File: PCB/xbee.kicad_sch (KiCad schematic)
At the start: 8 parts

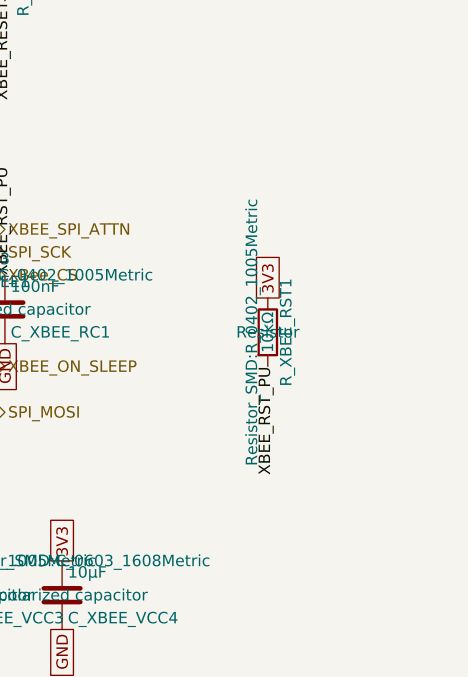
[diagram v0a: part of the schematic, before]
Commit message: fix: add pull-up on XBee SPI_ATTN pin
SPI_ATTN doubles as the XBee3's BOOTMODE strap; Digi's hardware
reference manual (doc 90001543) says not to let it be tied/pulled low
at reset. R_XBEE_ATTN_PU1 (10kΩ to 3V3) holds it high before firmware
configures the pin, matching the existing R_XBEE_RST1 pull-up pattern
on RESET.

Verified via kicad-cli: the new resistor lands on the XBEE_SPI_ATTN
net alongside U_XBEE1 pin 19 and the MCU's GPIO15, and ERC is clean.

Co-Authored-By: Claude Sonnet 5 <noreply@anthropic.com>
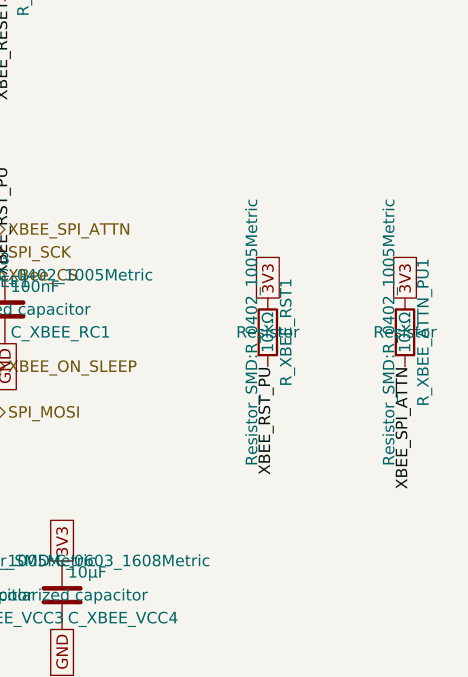
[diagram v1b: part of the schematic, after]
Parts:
- added R_XBEE_ATTN_PU1: 10kΩ, Resistor_SMD:R_0402_1005Metric, symbol Device:R
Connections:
- net 3V3: now also R_XBEE_ATTN_PU1.1
- net XBEE_SPI_ATTN: now also R_XBEE_ATTN_PU1.2
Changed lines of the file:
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@@
+		)
+	)
+	(label "XBEE_SPI_ATTN"
+		(at 210.82 114.3 270)
+		(effects
+			(font
+				(size 1.27 1.27)
+			)
+			(justify right)
 		)
 	)
@@
 		(property "Intersheetrefs" "${INTERSHEET_REFS}"
 			(at 195.58 106.68 0)
+			(hide yes)
+			(show_name no)
+			(do_not_autoplace no)
+			(effects
+				(font
+					(size 1.27 1.27)
+				)
+			)
+		)
+	)
+	(global_label "3V3"
+		(shape passive)
+		(at 210.82 106.68 90)
+		(fields_autoplaced yes)
+		(effects
+			(font
+				(size 1.27 1.27)
+			)
+			(justify left)
+		)
+		(property "Intersheetrefs" "${INTERSHEET_REFS}"
+			(at 210.82 106.68 0)
 			(hide yes)
 			(show_name no)
@@
 					(unit 1)
 				)
+			)
+		)
+	)
+	(symbol
+		(lib_id "Device:R")
+		(at 210.82 110.49 0)
+		(unit 1)
+		(body_style 1)
+		(exclude_from_sim no)
+		(in_bom yes)
+		(on_board yes)
+		(in_pos_files yes)
+		(dnp no)
+		(fields_autoplaced yes)
+		(property "Reference" "R_XBEE_ATTN_PU1"
+			(at 212.852 110.49 90)
+			(show_name no)
+			(do_not_autoplace no)
+			(effects
+				(font
+					(size 1.27 1.27)
+				)
+			)
+		)
+		(property "Value" "10kΩ"
+			(at 210.82 110.49 90)
+			(show_name no)
+			(do_not_autoplace no)
+			(effects
+				(font
+					(size 1.27 1.27)
+				)
+			)
+		)
+		(property "Footprint" "Resistor_SMD:R_0402_1005Metric"
+			(at 209.042 110.49 90)
+			(show_name no)
+			(do_not_autoplace no)
+			(effects
+				(font
+					(size 1.27 1.27)
+				)
+			)
+		)
+		(property "Datasheet" ""
+			(at 210.82 110.49 0)
+			(show_name no)
+			(do_not_autoplace no)
+			(effects
+				(font
+					(size 1.27 1.27)
+				)
+			)
+		)
+		(property "Description" "Resistor"
+			(at 210.82 110.49 0)
+			(show_name no)
+			(do_not_autoplace no)
+			(effects
+				(font
+					(size 1.27 1.27)
+				)
+			)
+		)
+		(property "MF" "Yageo"
+			(at 0 0 0)
+			(hide yes)
+			(show_name no)
+			(do_not_autoplace no)
+			(effects
+				(font
+					(size 1.27 1.27)
+				)
+			)
+		)
+		(property "Manufacturer_Part_Number" "RC0402FR-0710KL"
+			(at 0 0 0)
+			(hide yes)
+			(show_name no)
+			(do_not_autoplace no)
+			(effects
+				(font
+					(size 1.27 1.27)
+				)
+			)
+		)
+		(pin "1"
+		)
+		(pin "2"
+		)
+		(instances
+			(project "snips_controller"
+				(path "/21935953-32a0-46ad-8079-8177920c6978/4f95850f-f8fc-4b0b-b598-e710af0bb56d"
+					(reference "R_XBEE_ATTN_PU1")
+					(unit 1)
+				)

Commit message: task: write matched LCSC part numbers into the schematic
Adds scripts/apply_lcsc_fields.py, which clones each symbol's existing
Manufacturer_Part_Number property (same indentation/effects) into a new
'LCSC' field with the matched code -- the field name the Fabrication
Toolkit plugin already installed in this repo recognizes for JLCPCB BOM
matching.

Applied the 31 confirmed matches from jlc_match.py across all sheets
(68 individual references). C_BUCK_OUT1 and R_ISET1 are left without an
LCSC field -- JLC doesn't stock those exact Yageo part numbers, to be
sorted out separately.

Verified: kicad-cli sch export bom round-trips every LCSC value
correctly, and ERC reports 0 violations.

Also switched jlc_match.py's BOM export to unranged references so each
match maps cleanly to individual schematic symbols.

Co-Authored-By: Claude Sonnet 5 <noreply@anthropic.com>
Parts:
- C_XBEE_RC1, C_XBEE_VCC1: LCSC (none) -> C131394
- C_XBEE_VCC2: LCSC (none) -> C106215
- C_XBEE_VCC3: LCSC (none) -> C60137
- C_XBEE_VCC4: LCSC (none) -> C2936601
- R_XBEE_ATTN_PU1, R_XBEE_RST1: LCSC (none) -> C60490
- R_XBEE_RC1: LCSC (none) -> C106232
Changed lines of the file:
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@@
+			)
+		)
+		(property "LCSC" "C60137"
+			(at 0 0 0)
+			(hide yes)
+			(show_name no)
+			(do_not_autoplace no)
+			(effects
+				(font
+					(size 1.27 1.27)
+				)
 			)
 		)
@@
 			)
 		)
+		(property "LCSC" "C106215"
+			(at 0 0 0)
+			(hide yes)
+			(show_name no)
+			(do_not_autoplace no)
+			(effects
+				(font
+					(size 1.27 1.27)
+				)
+			)
+		)
 		(pin "1"
 		)
@@
 			)
 		)
+		(property "LCSC" "C2936601"
+			(at 0 0 0)
+			(hide yes)
+			(show_name no)
+			(do_not_autoplace no)
+			(effects
+				(font
+					(size 1.27 1.27)
+				)
+			)
+		)
 		(pin "1"
 		)
@@
 			)
 		)
+		(property "LCSC" "C131394"
+			(at 0 0 0)
+			(hide yes)
+			(show_name no)
+			(do_not_autoplace no)
+			(effects
+				(font
+					(size 1.27 1.27)
+				)
+			)
+		)
 		(pin "1"
 		)
@@
 			)
 		)
+		(property "LCSC" "C60490"
+			(at 0 0 0)
+			(hide yes)
+			(show_name no)
+			(do_not_autoplace no)
+			(effects
+				(font
+					(size 1.27 1.27)
+				)
+			)
+		)
 		(pin "1"
 		)
@@
 			)
 		)
+		(property "LCSC" "C60490"
+			(at 0 0 0)
+			(hide yes)
+			(show_name no)
+			(do_not_autoplace no)
+			(effects
+				(font
+					(size 1.27 1.27)
+				)
+			)
+		)
 		(pin "1"
 		)
@@
 			)
 		)
+		(property "LCSC" "C106232"
+			(at 0 0 0)
+			(hide yes)
+			(show_name no)
+			(do_not_autoplace no)
+			(effects
+				(font
+					(size 1.27 1.27)
+				)
+			)
+		)
 		(pin "1"
 		)
@@
 			(at 0 0 0)
 			(hide yes)
+			(show_name no)
+			(do_not_autoplace no)
+			(effects
+				(font
+					(size 1.27 1.27)
+				)
+			)
+		)
+		(property "LCSC" "C131394"
+			(at 0 0 0)
+			(hide yes)

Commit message: task: alert on Basic-library alternatives during JLC part matching (#33)
* task: alert on Basic-library alternatives during JLC part matching

JLC's "Extended" library carries a per-unique-part setup fee on top of
unit price; "Basic" doesn't. That fee doesn't amortize well on a board
with many distinct low-quantity parts -- confirmed the hard way: our
first real JLCPCB assembly quote came back at $333.84 vs PCBWay's
~$190 for the same order, and all 33 of our matched parts were
Extended.

jlc_match.py now does a secondary search for a same-value/same-package
Basic-library part whenever the real match lands on Extended, and
flags it in the report (new BasicAlt column + a Status alert) rather
than silently leaving it. On the current board this surfaces 11
plausible Basic-library swaps (common resistor/cap values, and the
generic 1N4148W diode and 2N7002 MOSFET, which are industry-standard
parts many brands stock identically).

This is alert-only, same as the rest of this script -- it doesn't
touch the schematic. Spot-checked 4 of the 11 suggestions directly
against JLC's catalog to confirm value/package actually match, not
just a keyword hit.

Co-Authored-By: Claude Sonnet 5 <noreply@anthropic.com>

* fix: two correctness bugs in Basic-library alternative matching

1. find_basic_alternative() trusted the raw keyword-search hit without
   verifying the candidate's actual value -- JLC's fuzzy full-text search
   can return a wrong-value part that just shares digits (e.g. searching
   "100 0402" surfaced a 1kΩ resistor, EIA code "1001", as a false match
   for a 100Ω part). Now parses and compares the actual numeric value
   (with unit) before accepting a candidate; falls back to exact
   model-name matching for non-numeric values (generic diode/transistor
   part families like "1N4148W", "2N7002").

2. The new value parser's regex required the unit to be the first
   character of the string, but JLC resistor descriptions carry a
   Chinese prefix ("厚膜电阻 10kΩ ±1%" = "thi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
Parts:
- C_XBEE_RC1, C_XBEE_VCC1: LCSC C131394 -> C1525; MF Yageo -> Samsung Electro-Mechanics; Manufacturer_Part_Number CC0402KRX7R9BB104 -> CL05B104KO5NNNC
- C_XBEE_VCC2: LCSC C106215 -> C15849; MF Yageo -> Samsung Electro-Mechanics; Manufacturer_Part_Number CC0603KRX5R7BB105 -> CL10A105KB8NNNC
- C_XBEE_VCC3: LCSC C60137 -> C1567; MF Yageo -> FH (Guangdong Fenghua Advanced Tech); Manufacturer_Part_Number CC0402JRNPO9BN470 -> 0402CG470J500NT
- C_XBEE_VCC4: LCSC C2936601 -> C19702; MF Yageo -> Samsung Electro-Mechanics; Manufacturer_Part_Number CC0603KRX5R7BB106 -> CL10A106KP8NNNC
- R_XBEE_ATTN_PU1, R_XBEE_RST1: LCSC C60490 -> C25744; MF Yageo -> UNI-ROYAL(Uniroyal Elec); Manufacturer_Part_Number RC0402FR-0710KL -> 0402WGF1002TCE
- R_XBEE_RC1: LCSC C106232 -> C25076; MF Yageo -> UNI-ROYAL(Uniroyal Elec); Manufacturer_Part_Number RC0402FR-07100RL -> 0402WGF1000TCE
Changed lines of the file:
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@@
 			)
 		)
-		(property "MF" "Yageo"
-			(at 0 0 0)
-			(hide yes)
-			(show_name no)
-			(do_not_autoplace no)
-			(effects
-				(font
-					(size 1.27 1.27)
-				)
-			)
-		)
-		(property "Manufacturer_Part_Number" "CC0402JRNPO9BN470"
-			(at 0 0 0)
-			(hide yes)
-			(show_name no)
-			(do_not_autoplace no)
-			(effects
-				(font
-					(size 1.27 1.27)
-				)
-			)
-		)
-		(property "LCSC" "C60137"
+		(property "MF" "FH (Guangdong Fenghua Advanced Tech)"
+			(at 0 0 0)
+			(hide yes)
+			(show_name no)
+			(do_not_autoplace no)
+			(effects
+				(font
+					(size 1.27 1.27)
+				)
+			)
+		)
+		(property "Manufacturer_Part_Number" "0402CG470J500NT"
+			(at 0 0 0)
+			(hide yes)
+			(show_name no)
+			(do_not_autoplace no)
+			(effects
+				(font
+					(size 1.27 1.27)
+				)
+			)
+		)
+		(property "LCSC" "C1567"
 			(at 0 0 0)
 			(hide yes)
@@
 			)
 		)
-		(property "MF" "Yageo"
-			(at 0 0 0)
-			(hide yes)
-			(show_name no)
-			(do_not_autoplace no)
-			(effects
-				(font
-					(size 1.27 1.27)
-				)
-			)
-		)
-		(property "Manufacturer_Part_Number" "CC0603KRX5R7BB105"
-			(at 0 0 0)
-			(hide yes)
-			(show_name no)
-			(do_not_autoplace no)
-			(effects
-				(font
-					(size 1.27 1.27)
-				)
-			)
-		)
-		(property "LCSC" "C106215"
+		(property "MF" "Samsung Electro-Mechanics"
+			(at 0 0 0)
+			(hide yes)
+			(show_name no)
+			(do_not_autoplace no)
+			(effects
+				(font
+					(size 1.27 1.27)
+				)
+			)
+		)
+		(property "Manufacturer_Part_Number" "CL10A105KB8NNNC"
+			(at 0 0 0)
+			(hide yes)
+			(show_name no)
+			(do_not_autoplace no)
+			(effects
+				(font
+					(size 1.27 1.27)
+				)
+			)
+		)
+		(property "LCSC" "C15849"
 			(at 0 0 0)
 			(hide yes)
@@
 			)
 		)
-		(property "MF" "Yageo"
-			(at 0 0 0)
-			(hide yes)
-			(show_name no)
-			(do_not_autoplace no)
-			(effects
-				(font
-					(size 1.27 1.27)
-				)
-			)
-		)
-		(property "Manufacturer_Part_Number" "CC0603KRX5R7BB106"
-			(at 0 0 0)
-			(hide yes)
-			(show_name no)
-			(do_not_autoplace no)
-			(effects
-				(font
-					(size 1.27 1.27)
-				)
-			)
-		)
-		(property "LCSC" "C2936601"
+		(property "MF" "Samsung Electro-Mechanics"
+			(at 0 0 0)
+			(hide yes)
+			(show_name no)
+			(do_not_autoplace no)
+			(effects
+				(font
+					(size 1.27 1.27)
+				)
+			)
+		)
+		(property "Manufacturer_Part_Number" "CL10A106KP8NNNC"
+			(at 0 0 0)
+			(hide yes)
+			(show_name no)
+			(do_not_autoplace no)
+			(effects
+				(font
+					(size 1.27 1.27)
+				)
+			)
+		)
+		(property "LCSC" "C19702"
 			(at 0 0 0)
 			(hide yes)
@@
 			)
 		)
-		(property "MF" "Yageo"
-			(at 0 0 0)
-			(hide yes)
-			(show_name no)
-			(do_not_autoplace no)
-			(effects
-				(font
-					(size 1.27 1.27)
-				)
-			)
-		)
-		(property "Manufacturer_Part_Number" "CC0402KRX7R9BB104"
-			(at 0 0 0)
-			(hide yes)
-			(show_name no)
-			(do_not_autoplace no)
-			(effects
-				(font
-					(size 1.27 1.27)
-				)
-			)
-		)
-		(property "LCSC" "C131394"
+		(property "MF" "Samsung Electro-Mechanics"
+			(at 0 0 0)
+			(hide yes)
+			(show_name no)
+			(do_not_autoplace no)
+			(effects
+				(font
+					(size 1.27 1.27)
+				)
+			)
+		)
+		(property "Manufacturer_Part_Number" "CL05B104KO5NNNC"
+			(at 0 0 0)
+			(hide yes)
+			(show_name no)
+			(do_not_autoplace no)
+			(effects
+				(font
+					(size 1.27 1.27)
+				)
+			)
+		)
+		(property "LCSC" "C1525"
 			(at 0 0 0)
 			(hide yes)
@@
 			)
 		)
-		(property "MF" "Yageo"
-			(at 0 0 0)
-			(hide yes)
-			(show_name no)
-			(do_not_autoplace no)
-			(effects
-				(font
-					(size 1.27 1.27)
-				)
-			)
-		)
-		(property "Manufacturer_Part_Number" "RC0402FR-0710KL"
-			(at 0 0 0)
-			(hide yes)
-			(show_name no)
-			(do_not_autoplace no)
-			(effects
-				(font
-					(size 1.27 1.27)
-				)
-			)
-		)
-		(property "LCSC" "C60490"
+		(property "MF" "UNI-ROYAL(Uniroyal Elec)"
+			(at 0 0 0)
+			(hide yes)
+			(show_name no)
+			(do_not_autoplace no)
+			(effects
+				(font
+					(size 1.27 1.27)
+				)
+			)
+		)
+		(property "Manufacturer_Part_Number" "0402WGF1002TCE"
+			(at 0 0 0)
+			(hide yes)
+			(show_name no)
+			(do_not_autoplace no)
+			(effects
+				(font
+					(size 1.27 1.27)
+				)
+			)
+		)
+		(property "LCSC" "C25744"
 			(at 0 0 0)
 			(hide yes)
@@
 			)
 		)
-		(property "MF" "Yageo"
-			(at 0 0 0)
-			(hide yes)
-			(show_name no)
-			(do_not_autoplace no)
-			(effects
-				(font
-					(size 1.27 1.27)
-				)
-			)
-		)
-		(property "Manufacturer_Part_Number" "RC0402FR-0710KL"
-			(at 0 0 0)
-			(hide yes)
-			(show_name no)
-			(do_not_autoplace no)
-			(effects
-				(font
-					(size 1.27 1.27)
-				)
-			)
-		)
-		(property "LCSC" "C60490"
+		(property "MF" "UNI-ROYAL(Uniroyal Elec)"
+			(at 0 0 0)
+			(hide yes)
+			(show_name no)
+			(do_not_autoplace no)
+			(effects
+				(font
+					(size 1.27 1.27)
+				)
+			)
+		)
+		(property "Manufacturer_Part_Number" "0402WGF1002TCE"
+			(at 0 0 0)
+			(hide yes)
+			(show_name no)
+			(do_not_autoplace no)
+			(effects
+				(font
+					(size 1.27 1.27)
+				)
+			)
+		)
+		(property "LCSC" "C25744"
 			(at 0 0 0)
 			(hide yes)
@@
 			)
 		)
-		(property "MF" "Yageo"
-			(at 0 0 0)
-			(hide yes)
-			(show_name no)
-			(do_not_autoplace no)
-			(effects
-				(font
-					(size 1.27 1.27)
-				)
-			)
-		)
-		(property "Manufacturer_Part_Number" "RC0402FR-07100RL"
-			(at 0 0 0)
-			(hide yes)
-			(show_name no)
-			(do_not_autoplace no)
-			(effects
-				(font
-					(size 1.27 1.27)
-				)
-			)
-		)
-		(property "LCSC" "C106232"
+		(property "MF" "UNI-ROYAL(Uniroyal Elec)"
+			(at 0 0 0)
+			(hide yes)
+			(show_name no)
+			(do_not_autoplace no)
+			(effects
+				(font
+					(size 1.27 1.27)
+				)
+			)
+		)
+		(property "Manufacturer_Part_Number" "0402WGF1000TCE"
+			(at 0 0 0)
+			(hide yes)
+			(show_name no)
+			(do_not_autoplace no)
+			(effects
+				(font
+					(size 1.27 1.27)
+				)
+			)
+		)
+		(property "LCSC" "C25076"
 			(at 0 0 0)
 			(hide yes)
@@
 			)
 		)
-		(property "MF" "Yageo"
-			(at 0 0 0)
-			(hide yes)
-			(show_name no)
-			(do_not_autoplace no)
-			(effects
-				(font
-					(size 1.27 1.27)
-				)
-			)
-		)
-		(property "Manufacturer_Part_Number" "CC0402KRX7R9BB104"
-			(at 0 0 0)
-			(hide yes)
-			(show_name no)
-			(do_not_autoplace no)
-			(effects
-				(font
-					(size 1.27 1.27)
-				)
-			)
-		)
-		(property "LCSC" "C131394"
-			(at 0 0 0)
-			(hide yes)
+		(property "MF" "Samsung Electro-Mechanics"
+			(at 0 0 0)
+			(hide yes)
+			(show_name no)
+			(do_not_autoplace no)
+			(effects
+				(font
+					(size 1.27 1.27)
+				)
+			)
+		)
+		(property "Manufacturer_Part_Number" "CL05B104KO5NNNC"
+			(at 0 0 0)
+			(hide yes)
+			(show_name no)
+			(do_not_autoplace no)
+			(effects
+				(font
+					(size 1.27 1.27)
+				)
+			)
+		)
+		(property "LCSC" "C1525"
+			(at 0 0 0)
+			(hide yes)
